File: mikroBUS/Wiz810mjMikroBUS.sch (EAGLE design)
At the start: 3 parts

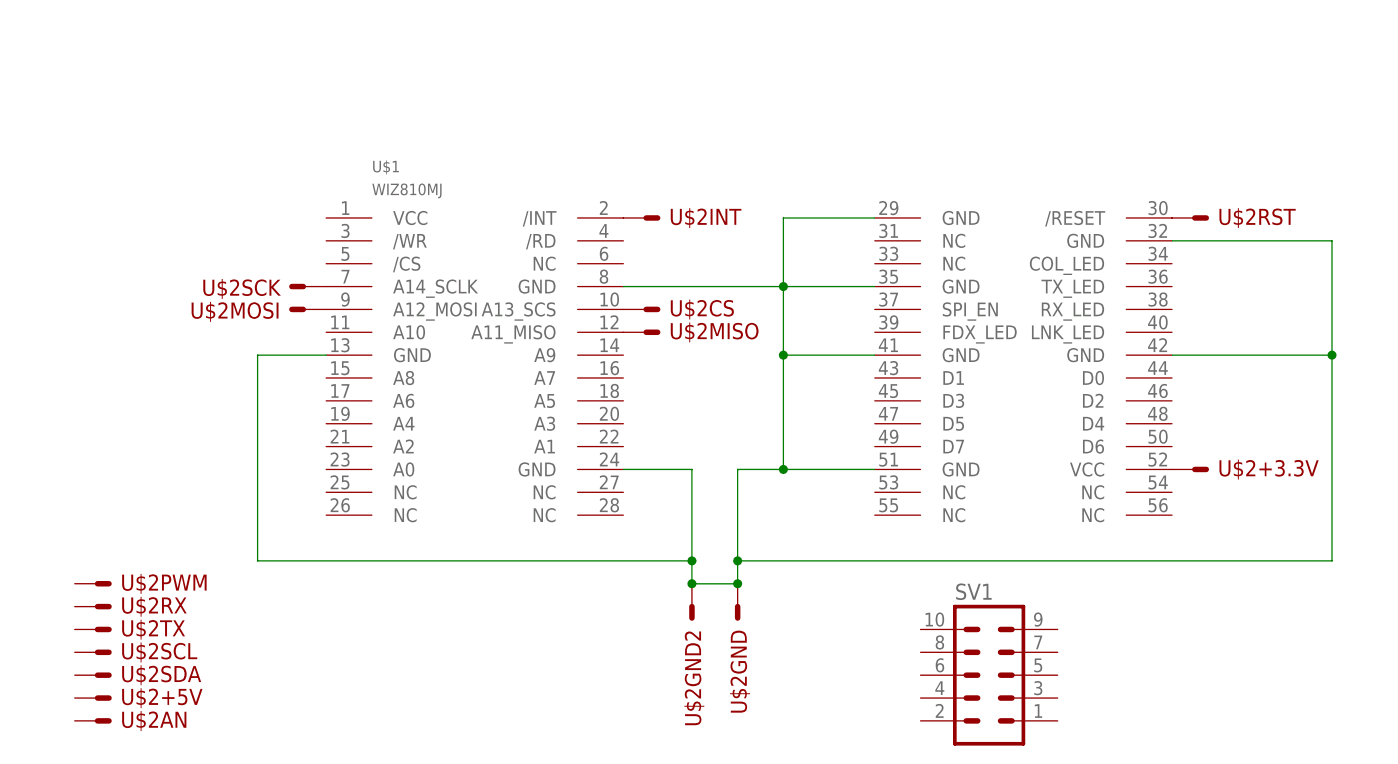
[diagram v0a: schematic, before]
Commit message: 
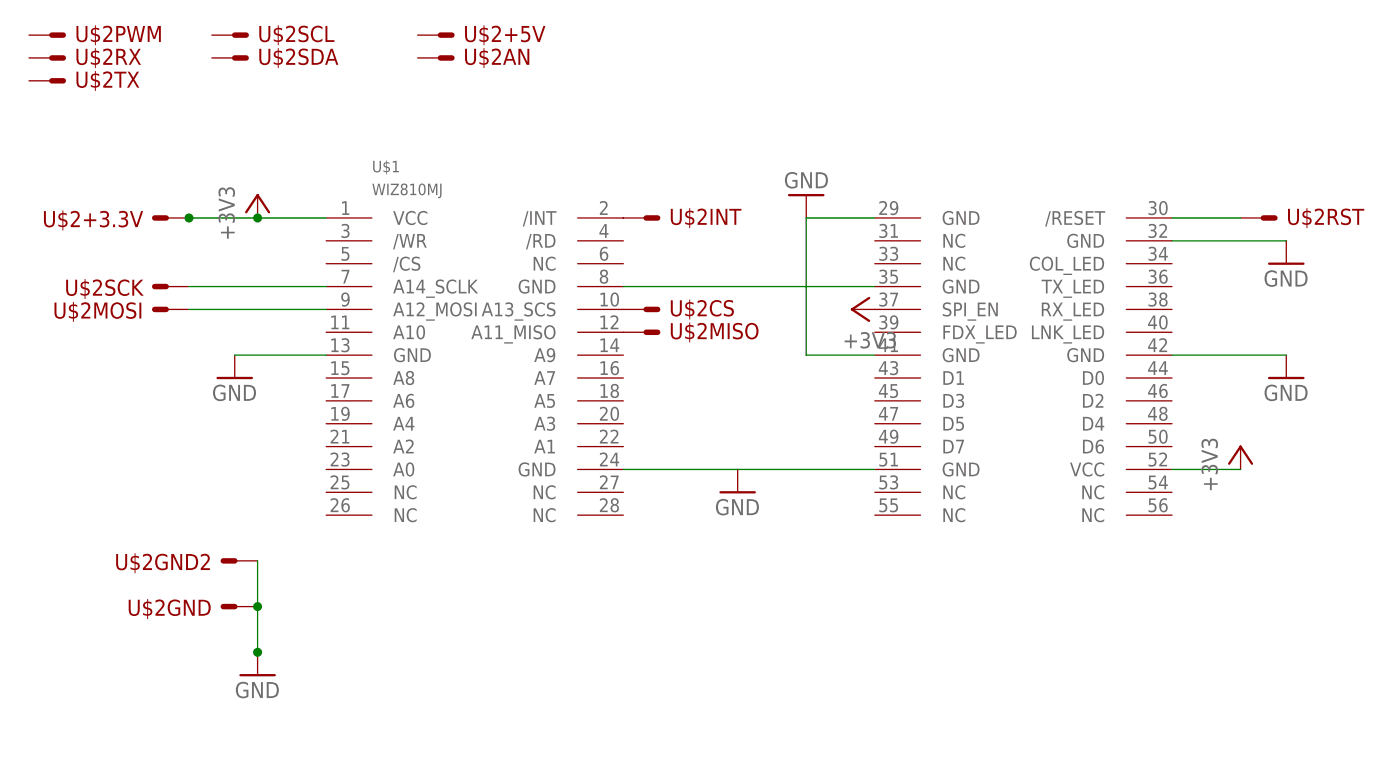
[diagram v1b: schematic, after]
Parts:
- removed SV1: (no value), con-lstb:MA05-2
- U$2: device lieven:MIKROBUS -> lieven:MIKROBUSSIL
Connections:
- net N$3 renamed GND
- removed net N$9: U$1.VCC@1, U$2+3.3V.S
- new net +3V3: U$1.SPI_EN, U$1.VCC, U$1.VCC@1, U$2+3.3V.S
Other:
- moved on the sheet: U$2+3.3V, U$2+5V, U$2AN, U$2GND, U$2GND2, U$2MOSI, U$2PWM, U$2RST, U$2RX, U$2SCK, U$2SCL, U$2SDA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
